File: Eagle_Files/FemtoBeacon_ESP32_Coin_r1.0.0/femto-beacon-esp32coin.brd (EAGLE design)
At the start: 25.4 x 29.2 mm, 48 parts, among them IC1 ESP32-QFN_5X5

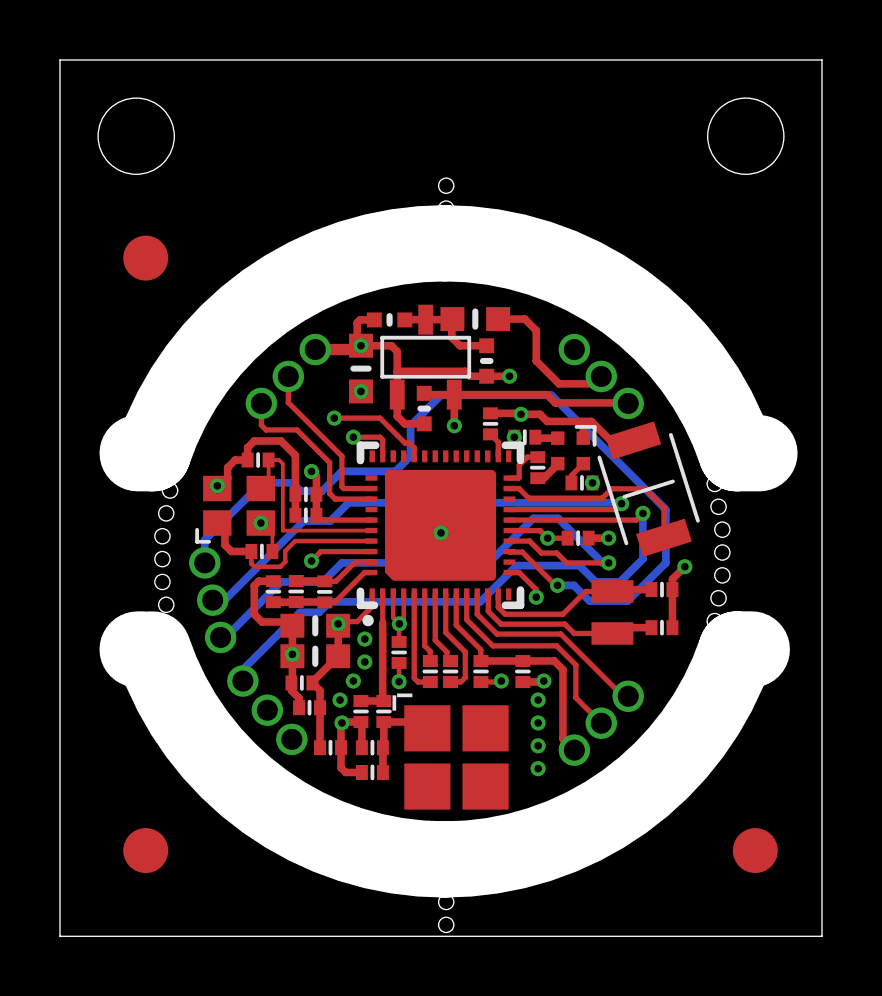
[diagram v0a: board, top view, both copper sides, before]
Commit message: Fixing solder stop mask on femto-beacon-esp32coin and femto-beacon-esp32-lps. Adding Blender3D model of stencil jig for the coin
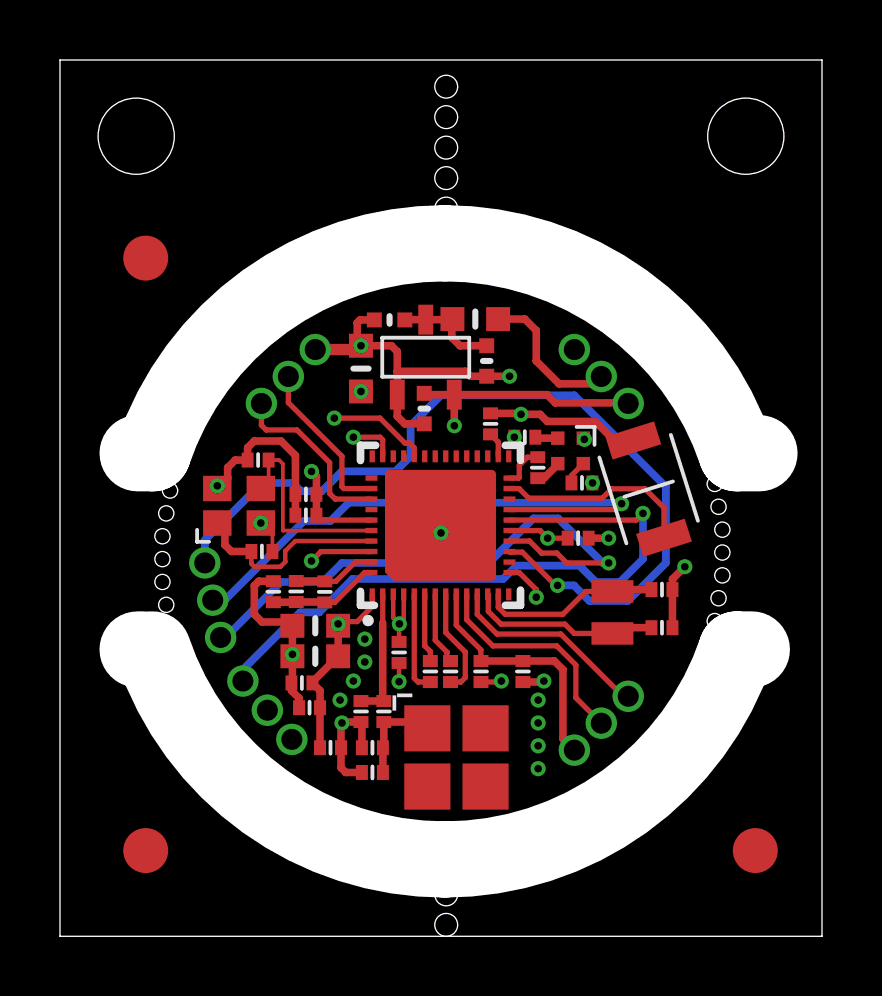
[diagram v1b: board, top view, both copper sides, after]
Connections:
- net 3.3V: now also RGB1.1
- net GND: no longer RGB1.1
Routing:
- net 3.3V: track 58.3 -> 60.6 mm, vias 8 -> 9
- net GND: track 82.6 -> 82.0 mm
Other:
- board text added: "1.0.1"
- board text added: "Coin is 18mm dia."
- board text added: "EN"
- board text added: "IO34"
- board text added: "IO35"
- board text removed: "1.0.0"
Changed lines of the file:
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@@
 <setting verticaltext="up"/>
 </settings>
-<grid distance="50" unitdist="mil" unit="mil" style="dots" multiple="1" display="yes" altdistance="5" altunitdist="mil" altunit="mil"/>
+<grid distance="5" unitdist="mil" unit="mil" style="dots" multiple="1" display="yes" altdistance="5" altunitdist="mil" altunit="mil"/>
 <layers>
 <layer number="1" name="Top" color="4" fill="1" visible="yes" active="yes"/>
@@
 <layer number="30" name="bStop" color="7" fill="6" visible="no" active="yes"/>
 <layer number="31" name="tCream" color="7" fill="4" visible="yes" active="yes"/>
-<layer number="32" name="bCream" color="7" fill="5" visible="no" active="yes"/>
+<layer number="32" name="bCream" color="7" fill="5" visible="yes" active="yes"/>
 <layer number="33" name="tFinish" color="6" fill="3" visible="no" active="yes"/>
 <layer number="34" name="bFinish" color="6" fill="6" visible="no" active="yes"/>
@@
 <layer number="45" name="Holes" color="7" fill="1" visible="yes" active="yes"/>
 <layer number="46" name="Milling" color="3" fill="1" visible="yes" active="yes"/>
-<layer number="47" name="Measures" color="7" fill="1" visible="no" active="yes"/>
+<layer number="47" name="Measures" color="7" fill="1" visible="yes" active="yes"/>
 <layer number="48" name="Document" color="7" fill="1" visible="yes" active="yes"/>
 <layer number="49" name="Reference" color="7" fill="1" visible="yes" active="yes"/>
@@
 <text x="20.574" y="10.922" size="0.8128" layer="22" font="vector" ratio="20" rot="MR0" align="center-left">FemtoBeacon</text>
 <text x="20.066" y="9.652" size="0.8128" layer="22" font="vector" ratio="20" rot="MR0" align="center-left">ESP32 Coin</text>
-<text x="13.208" y="5.842" size="0.8128" layer="22" font="vector" ratio="20" rot="MR0" align="center">1.0.0</text>
+<text x="13.208" y="5.842" size="0.8128" layer="22" font="vector" ratio="20" rot="MR0" align="center">1.0.1</text>
 <text x="12.954" y="15.24" size="0.8128" layer="22" font="vector" ratio="20" rot="MR0" align="center">IO26=R</text>
 <text x="12.954" y="14.224" size="0.8128" layer="22" font="vector" ratio="20" rot="MR0" align="center">IO4=G</text>
@@
 <hole x="3.6685" y="14.859" drill="0.508"/>
 <hole x="3.5415" y="14.097" drill="0.508"/>
-<hole x="12.8735" y="0.381" drill="0.508"/>
-<hole x="12.8735" y="1.143" drill="0.508"/>
-<hole x="12.8735" y="25.019" drill="0.508"/>
-<hole x="12.8735" y="24.257" drill="0.508"/>
+<hole x="12.8735" y="0.381" drill="0.762"/>
+<hole x="12.8735" y="24.257" drill="0.762"/>
 <hole x="22.86" y="26.67" drill="2.54"/>
 <hole x="2.54" y="26.67" drill="2.54"/>
@@
 <vertex x="21.717" y="26.67" curve="90"/>
 </polygon>
+<text x="18.288" y="8.636" size="0.6096" layer="22" font="vector" ratio="20" rot="MR0" align="center-left">IO35</text>
+<text x="17.399" y="7.747" size="0.6096" layer="22" font="vector" ratio="20" rot="MR0" align="center-left">IO34</text>
+<text x="16.51" y="6.858" size="0.6096" layer="22" font="vector" ratio="20" rot="MR0" align="center-left">EN</text>
+<hole x="12.8735" y="1.397" drill="0.762"/>
+<hole x="12.8735" y="25.273" drill="0.762"/>
+<hole x="12.8735" y="26.289" drill="0.762"/>
+<hole x="12.8735" y="27.305" drill="0.762"/>
+<hole x="12.8735" y="28.321" drill="0.762"/>
+<dimension x1="0" y1="0" x2="0" y2="29.21" x3="-9.144" y3="14.605" textsize="1.778" layer="47" dtype="vertical" visible="yes"/>
+<dimension x1="0" y1="29.21" x2="25.4" y2="29.21" x3="12.7" y3="44.577" textsize="1.778" layer="47" dtype="vertical" visible="yes"/>
+<dimension x1="1.27" y1="26.67" x2="3.81" y2="26.67" x3="2.54" y3="30.734" textsize="1.778" layer="47" dtype="diameter" visible="yes"/>
+<dimension x1="2.54" y1="26.67" x2="0" y2="26.543" x3="1.27" y3="34.163" textsize="1.778" layer="47" dtype="horizontal" visible="yes"/>
+<dimension x1="2.54" y1="26.67" x2="22.86" y2="26.67" x3="12.7" y3="38.735" textsize="1.778" layer="47" dtype="horizontal" visible="yes"/>
+<dimension x1="0" y1="0" x2="2.54" y2="26.67" x3="-5.461" y3="13.335" textsize="1.778" layer="47" dtype="vertical" visible="yes"/>
+<text x="3.302" y="-3.175" size="1.778" layer="47">Coin is 18mm dia.</text>
 </plain>
 <attributes>
@@
 <wire x1="10.033" y1="19.558" x2="8.509" y2="19.558" width="0.381" layer="1"/>
 <contactref element="BOOT1" pad="1"/>
-<wire x1="19.1103" y1="16.52681875" x2="18.3483" y2="16.52681875" width="0.254" layer="1"/>
-<wire x1="18.3483" y1="16.52681875" x2="17.7133" y2="17.16181875" width="0.254" layer="1"/>
-<wire x1="17.7133" y1="17.16181875" x2="17.272" y2="17.16181875" width="0.254" layer="1"/>
-<wire x1="17.272" y1="17.16181875" x2="16.23918125" y2="17.16181875" width="0.254" layer="1"/>
+<wire x1="19.1103" y1="16.52681875" x2="18.4753" y2="16.52681875" width="0.254" layer="1"/>
+<wire x1="18.4753" y1="16.52681875" x2="17.8403" y2="17.16181875" width="0.254" layer="1"/>
+<wire x1="17.8403" y1="17.16181875" x2="16.23918125" y2="17.16181875" width="0.254" layer="1"/>
 <wire x1="16.23918125" y1="17.16181875" x2="16.002" y2="17.399" width="0.254" layer="1"/>
 <wire x1="16.002" y1="17.399" x2="15.367" y2="17.399" width="0.254" layer="1"/>
@@
 <wire x1="7.747" y1="9.3345" x2="7.747" y2="9.398" width="0.254" layer="1"/>
 <wire x1="12.7" y1="13.445" x2="12.7" y2="8.4889" width="0.381" layer="2"/>
-<contactref element="RGB1" pad="1"/>
-<wire x1="17.443" y1="16.6048" x2="17.443" y2="16.99081875" width="0.254" layer="1"/>
-<wire x1="17.443" y1="16.99081875" x2="17.272" y2="17.16181875" width="0.254" layer="1"/>
 <contactref element="PIN_GPIO_A" pad="P$3"/>
 <wire x1="7.728678125" y1="6.563246875" x2="7.960246875" y2="6.563246875" width="0.381" layer="2"/>
@@
 <wire x1="8.636" y1="9.779" x2="9.271" y2="10.414" width="0.381" layer="15"/>
 <wire x1="7.504215625" y1="8.128" x2="8.636" y2="8.128" width="0.381" layer="15"/>
+<contactref element="RGB1" pad="1"/>
+<wire x1="17.4784" y1="16.564" x2="17.443" y2="16.5994" width="0.254" layer="1"/>
+<wire x1="17.443" y1="16.6048" x2="17.443" y2="16.5994" width="0.254" layer="1"/>
+<via x="17.4784" y="16.564" extent="1-16" drill="0.254" diameter="0.508"/>
+<wire x1="17.4784" y1="16.564" x2="17.4784" y2="17.0974" width="0.381" layer="15"/>
+<wire x1="17.4784" y1="17.0974" x2="17.78" y2="17.399" width="0.381" layer="15"/>
+<wire x1="17.78" y1="17.399" x2="18.578103125" y2="17.399" width="0.381" layer="15"/>
+<wire x1="18.578103125" y1="17.399" x2="18.94105" y2="17.761946875" width="0.381" layer="15"/>
 </signal>
 <signal name="VIN_PIN">
@@
 <wire x1="17.653" y1="11.176" x2="18.923" y2="11.176" width="0.254" layer="16"/>
 <wire x1="18.923" y1="11.176" x2="20.193" y2="12.446" width="0.254" layer="16"/>
-<wire x1="20.193" y1="12.446" x2="20.193" y2="14.224" width="0.254" layer="16"/>
+<wire x1="20.193" y1="12.446" x2="20.193" y2="14.986" width="0.254" layer="16"/>
 <wire x1="4.826" y1="13.208" x2="6.731" y2="15.113" width="0.254" layer="16"/>
 <wire x1="4.826" y1="12.446" x2="4.826" y2="13.208" width="0.254" layer="16"/>
@@
 <wire x1="11.684" y1="16.002" x2="11.176" y2="15.494" width="0.254" layer="16"/>
 <wire x1="11.176" y1="15.494" x2="9.39034375" y2="15.494" width="0.254" layer="16"/>
-<wire x1="20.193" y1="14.224" x2="16.383" y2="18.034" width="0.254" layer="16"/>
-<wire x1="16.383" y1="18.034" x2="12.7" y2="18.034" width="0.254" layer="16"/>
+<wire x1="20.193" y1="14.986" x2="17.145" y2="18.034" width="0.254" layer="16"/>
+<wire x1="17.145" y1="18.034" x2="12.7" y2="18.034" width="0.254" layer="16"/>
 <wire x1="12.7" y1="18.034" x2="11.684" y2="17.018" width="0.254" layer="16"/>
 </signal>
@@
 <wire x1="17.85928125" y1="11.811" x2="18.669" y2="11.811" width="0.254" layer="16"/>
 <wire x1="17.31318125" y1="12.3571" x2="17.85928125" y2="11.811" width="0.254" layer="16"/>
-<wire x1="14.0137875" y1="11.15059375" x2="8.99159375" y2="11.15059375" width="0.254" layer="16"/>
-<wire x1="14.0137875" y1="11.15059375" x2="15.22029375" y2="12.3571" width="0.254" layer="16"/>
+<wire x1="14.7757875" y1="11.91259375" x2="9.75359375" y2="11.91259375" width="0.254" layer="16"/>
+<wire x1="14.7757875" y1="11.91259375" x2="15.22029375" y2="12.3571" width="0.254" layer="16"/>
 <wire x1="18.669" y1="11.811" x2="19.431" y2="12.573" width="0.254" layer="16"/>
 <wire x1="19.431" y1="12.573" x2="19.431" y2="14.097" width="0.254" layer="16"/>
-<wire x1="8.99159375" y1="11.15059375" x2="8.636" y2="10.795" width="0.254" layer="16"/>
+<wire x1="9.75359375" y1="11.91259375" x2="8.636" y2="10.795" width="0.254" layer="16"/>
 <wire x1="8.636" y1="10.795" x2="8.001" y2="10.795" width="0.254" layer="16"/>
 <wire x1="8.001" y1="10.795" x2="6.096" y2="8.89" width="0.254" layer="16"/>

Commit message: Setting correct ESP32 chip for the coin design to ESP32‑D2WD as it has 2MiB of internal Flash
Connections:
- net EN renamed RESET
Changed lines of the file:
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@@
 <setting verticaltext="up"/>
 </settings>
-<grid distance="5" unitdist="mil" unit="mil" style="dots" multiple="1" display="yes" altdistance="5" altunitdist="mil" altunit="mil"/>
+<grid distance="2" unitdist="mil" unit="mil" style="dots" multiple="1" display="yes" altdistance="5" altunitdist="mil" altunit="mil"/>
 <layers>
 <layer number="1" name="Top" color="4" fill="1" visible="yes" active="yes"/>
@@
 <elements>
 <element name="IC1" library="esp32-wroom-32" package="ESP32-QFN48_5X5" value="ESP32-QFN_5X5" x="12.683" y="13.699" smashed="yes">
-<attribute name="MPN" value="ESP32-S0WD" x="12.683" y="13.699" size="1.778" layer="27" display="off"/>
+<attribute name="MPN" value="ESP32-D2WD" x="12.683" y="13.699" size="1.778" layer="27" display="off"/>
 </element>
 <element name="C6" library="parts_0201" package="PART" value="270pF" x="12.3444" y="8.8265" smashed="yes" rot="R90">
@@
 <wire x1="19.5016" y1="14.9154" x2="20.132696875" y2="14.284303125" width="0.1778" layer="1"/>
 </signal>
-<signal name="EN">
+<signal name="RESET">
 <contactref element="IC1" pad="9"/>
 <contactref element="C22" pad="2"/>

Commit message: Current work on Hacker House board, and ESP32 coins
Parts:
- FB1, FB2: value (none) -> FERRITE
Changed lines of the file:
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@@
 <attribute name="MPN" value="GRM033C80J104KE84D" x="9.017" y="6.2865" size="1.778" layer="27" rot="R180" display="off"/>
 </element>
-<element name="FB1" library="microbuilder" package="_0603MP" value="" x="10.033" y="18.923" smashed="yes" rot="R90">
+<element name="FB1" library="microbuilder" package="_0603MP" value="FERRITE" x="10.033" y="18.923" smashed="yes" rot="R90">
 <attribute name="MPN" value="BLM18RK102SN1D" x="10.033" y="18.923" size="0.6096" layer="27" font="vector" ratio="20" rot="R90" display="off"/>
-<attribute name="VALUE" x="10.9855" y="17.9705" size="0.4064" layer="27" ratio="10" rot="R90"/>
 </element>
-<element name="FB2" library="microbuilder" package="_0603MP" value="" x="13.843" y="20.574" smashed="yes">
+<element name="FB2" library="microbuilder" package="_0603MP" value="FERRITE" x="13.843" y="20.574" smashed="yes">
 <attribute name="MPN" value="BLM18RK102SN1D" x="13.843" y="20.574" size="0.6096" layer="27" font="vector" ratio="20" display="off"/>
-<attribute name="VALUE" x="12.8905" y="19.6215" size="0.4064" layer="27" ratio="10"/>
 </element>
 <element name="C14" library="microbuilder" package="_0402MP" value="0.47uF" x="14.224" y="19.177" smashed="yes" rot="R90">
